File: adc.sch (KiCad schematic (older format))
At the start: 19 parts, among them J15 Conn_01x04_Male, U22 AD7960BCPZ-RL7, U23 OPA325

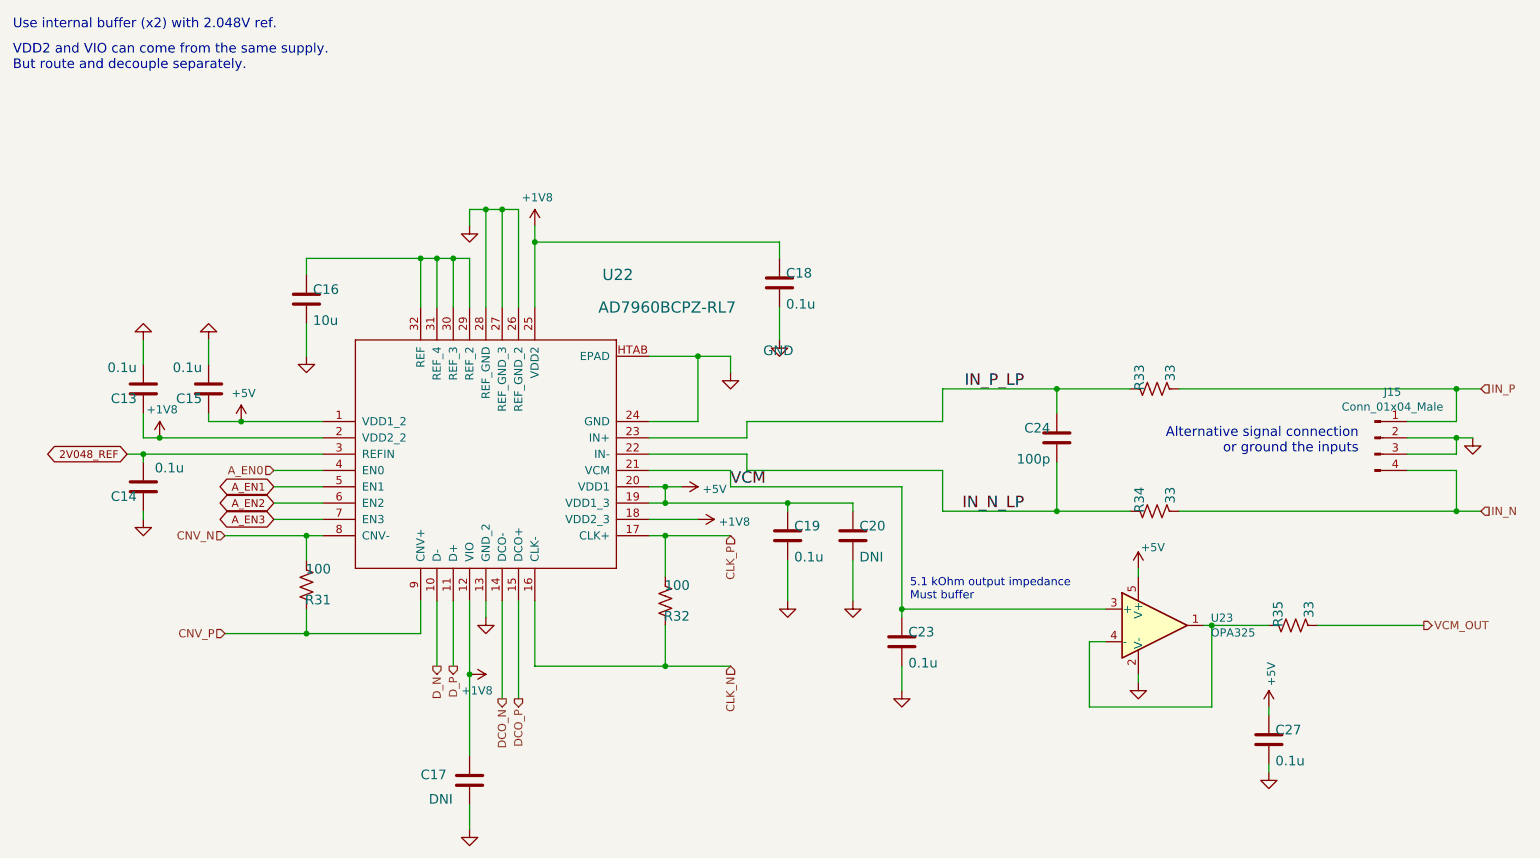
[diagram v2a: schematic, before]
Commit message: layout cleanup; removed custom footrpints
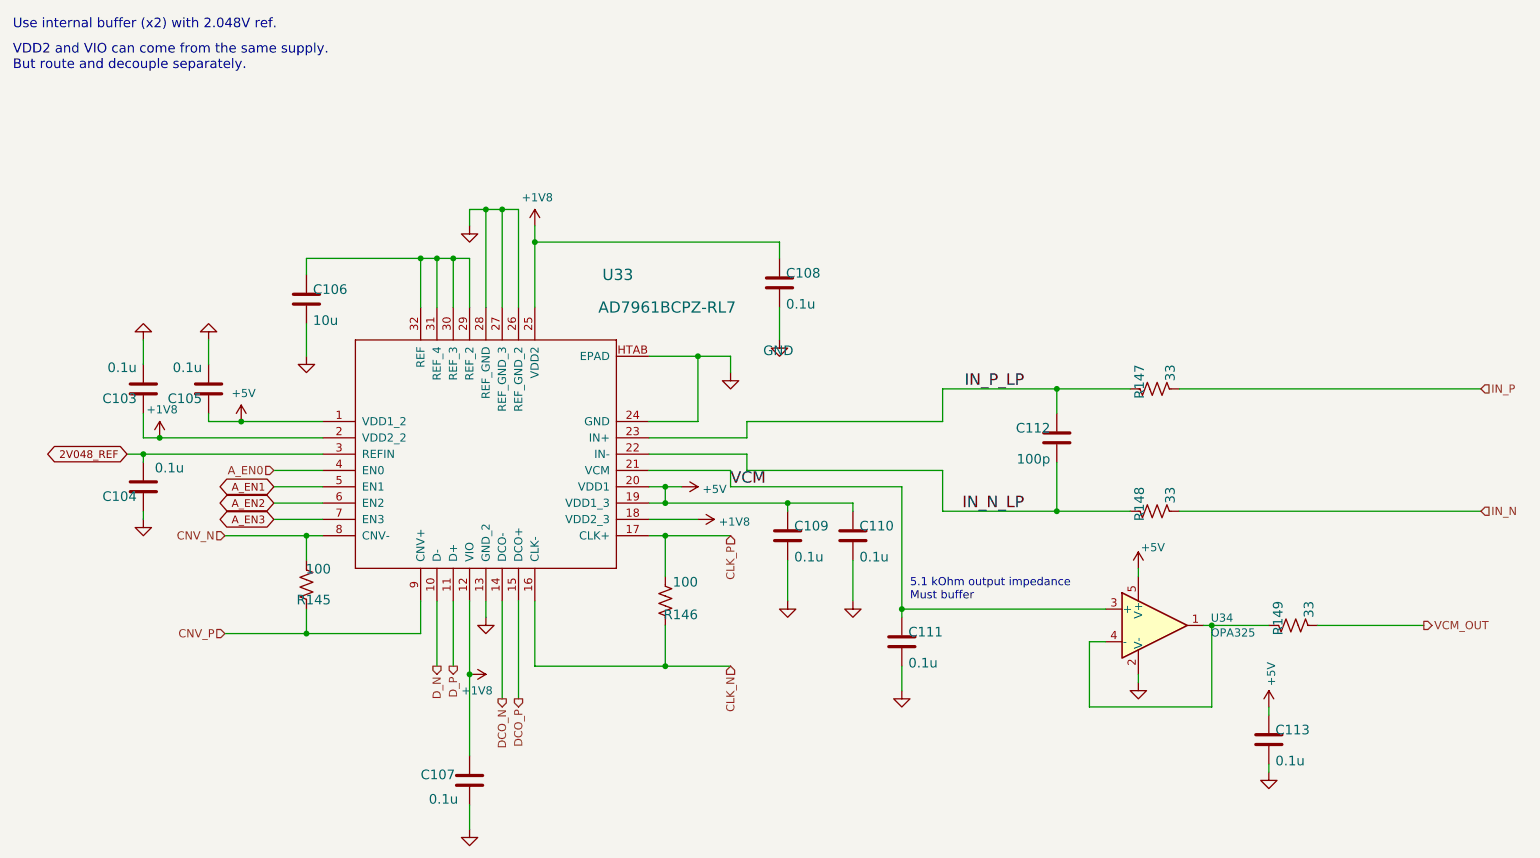
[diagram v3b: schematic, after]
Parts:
- removed J15: Conn_01x04_Male, Connector_PinHeader_2.54mm:PinHeader_1x04_P2.54mm_Vertical_SMD_Pin1Left, symbol Connector:Conn_01x04_Male
- C17, C20: value DNI -> 0.1u; Manf# (none) -> CL10B104KA8NFNC
- U22: value AD7960BCPZ-RL7 -> AD7961BCPZ-RL7; footprint adc_dac_v1:CP_32_7 -> Package_DFN_QFN:QFN-32-1EP_5x5mm_P0.5mm_EP3.1x3.1mm
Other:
- note removed: "Alternative signal connection\nor ground the inputs"
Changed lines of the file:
@@
 $Descr A 11000 8500
 encoding utf-8
-Sheet 6 18
+Sheet 8 18
 Title ""
 Date ""
@@
 AR Path="/60BF7757/B0DC2316" Ref="C69"  Part="1"
 AR Path="/60C1F416/B0DC2316" Ref="C112"  Part="1"
-F 0 "C24" H 7090 3725 59  0000 L BNN
+F 0 "C112" H 7090 3725 59  0000 L BNN
 F 1 "100p" H 7090 3535 59  0000 L BNN
 F 2 "Capacitor_SMD:C_0603_1608Metric" H 7050 3700 50  0001 C CNN
@@
 AR Path="/60BF7757/B996151F" Ref="R140"  Part="1"
 AR Path="/60C1F416/B996151F" Ref="R145"  Part="1"
-F 0 "R31" H 2300 4659 59  0000 L BNN
+F 0 "R145" H 2300 4659 59  0000 L BNN
 F 1 "100" H 2300 4470 59  0000 L BNN
 F 2 "Resistor_SMD:R_0603_1608Metric" H 2450 4600 50  0001 C CNN
@@
 AR Path="/60BF7757/56DFCCD0" Ref="C65"  Part="1"
 AR Path="/60C1F416/56DFCCD0" Ref="C108"  Part="1"
-F 0 "C18" H 5390 2775 59  0000 L BNN
+F 0 "C108" H 5390 2775 59  0000 L BNN
 F 1 "0.1u" H 5390 2585 59  0000 L BNN
 F 2 "Capacitor_SMD:C_0603_1608Metric" H 5350 2750 50  0001 C CNN
@@
 AR Path="/60BF7757/BF33D434" Ref="R141"  Part="1"
 AR Path="/60C1F416/BF33D434" Ref="R146"  Part="1"
-F 0 "R32" H 4500 4759 59  0000 L BNN
-F 1 "100" H 4500 4570 59  0000 L BNN
+F 0 "R146" H 4450 4750 59  0000 L BNN
+F 1 "100" H 4450 4550 59  0000 L BNN
 F 2 "Resistor_SMD:R_0603_1608Metric" H 4650 4700 50  0001 C CNN
 F 3 "" H 4650 4700 50  0001 C CNN
@@
 AR Path="/60BF7757/C9238E33" Ref="C66"  Part="1"
 AR Path="/60C1F416/C9238E33" Ref="C109"  Part="1"
-F 0 "C19" H 5440 4325 59  0000 L BNN
+F 0 "C109" H 5440 4325 59  0000 L BNN
 F 1 "0.1u" H 5440 4135 59  0000 L BNN
 F 2 "Capacitor_SMD:C_0603_1608Metric" H 5400 4300 50  0001 C CNN
@@
 AR Path="/60BF7757/E612D2BB" Ref="C67"  Part="1"
 AR Path="/60C1F416/E612D2BB" Ref="C110"  Part="1"
-F 0 "C20" H 5840 4325 59  0000 L BNN
-F 1 "DNI" H 5840 4135 59  0000 L BNN
+F 0 "C110" H 5840 4325 59  0000 L BNN
+F 1 "0.1u" H 5840 4135 59  0000 L BNN
 F 2 "Capacitor_SMD:C_0603_1608Metric" H 5800 4300 50  0001 C CNN
 F 3 "" H 5800 4300 50  0001 C CNN
+F 4 "CL10B104KA8NFNC" H 5800 4300 50  0001 C CNN "Manf#"
 	1    5800 4300
 	1    0    0    -1
@@
 AR Path="/60BF7757/1FADEAAB" Ref="C60"  Part="1"
 AR Path="/60C1F416/1FADEAAB" Ref="C103"  Part="1"
-F 0 "C13" H 1490 3425 59  0000 L BNN
+F 0 "C103" H 1490 3425 59  0000 L BNN
 F 1 "0.1u" H 1490 3235 59  0000 L BNN
 F 2 "Capacitor_SMD:C_0603_1608Metric" H 1450 3400 50  0001 C CNN
@@
 AR Path="/60BF7757/9D5B9004" Ref="C62"  Part="1"
 AR Path="/60C1F416/9D5B9004" Ref="C105"  Part="1"
-F 0 "C15" H 1890 3425 59  0000 L BNN
+F 0 "C105" H 1890 3425 59  0000 L BNN
 F 1 "0.1u" H 1890 3235 59  0000 L BNN
 F 2 "Capacitor_SMD:C_0603_1608Metric" H 1850 3400 50  0001 C CNN
@@
 AR Path="/60BF7757/87DF8B8E" Ref="R142"  Part="1"
 AR Path="/60C1F416/87DF8B8E" Ref="R147"  Part="1"
-F 0 "R33" H 7500 3459 59  0000 L BNN
+F 0 "R147" H 7500 3459 59  0000 L BNN
 F 1 "33" H 7500 3270 59  0000 L BNN
 F 2 "Resistor_SMD:R_0603_1608Metric" H 7650 3400 50  0001 C CNN
@@
 AR Path="/60BF7757/BFC3FA38" Ref="R143"  Part="1"
 AR Path="/60C1F416/BFC3FA38" Ref="R148"  Part="1"
-F 0 "R34" H 7500 4209 59  0000 L BNN
+F 0 "R148" H 7500 4209 59  0000 L BNN
 F 1 "33" H 7500 4020 59  0000 L BNN
 F 2 "Resistor_SMD:R_0603_1608Metric" H 7650 4150 50  0001 C CNN
@@
 $EndComp
 $Comp
-L power:GND #GND0124
-U 1 1 5F8B303C
-P 9600 3700
-AR Path="/6095A697/5F8B303C" Ref="#GND0124"  Part="1"
-AR Path="/60BE6CE5/5F8B303C" Ref="#GND0217"  Part="1"
-AR Path="/60BF7757/5F8B303C" Ref="#GND0232"  Part="1"
-AR Path="/60C1F416/5F8B303C" Ref="#GND0247"  Part="1"
-F 0 "#GND0247" H 9600 3700 50  0001 C CNN
-F 1 "GND" H 9500 3600 59  0001 L BNN
-F 2 "" H 9600 3700 50  0001 C CNN
-F 3 "" H 9600 3700 50  0001 C CNN
-	1    9600 3700
-	-1   0    0    -1
-$EndComp
-$Comp
 L Device:C C17
 U 1 1 E8572435
@@
 AR Path="/60BF7757/E8572435" Ref="C64"  Part="1"
 AR Path="/60C1F416/E8572435" Ref="C107"  Part="1"
-F 0 "C17" H 3150 5800 59  0000 L BNN
-F 1 "DNI" H 3200 5650 59  0000 L BNN
+F 0 "C107" H 3150 5800 59  0000 L BNN
+F 1 "0.1u" H 3200 5650 59  0000 L BNN
 F 2 "Capacitor_SMD:C_0603_1608Metric" H 3450 5800 50  0001 C CNN
 F 3 "" H 3450 5800 50  0001 C CNN
+F 4 "CL10B104KA8NFNC" H 3450 5800 50  0001 C CNN "Manf#"
 	1    3450 5800
 	1    0    0    -1
@@
 AR Path="/60BF7757/70C280EF" Ref="U31"  Part="1"
 AR Path="/60C1F416/70C280EF" Ref="U33"  Part="1"
-F 0 "U22" H 4264 4859 69  0000 L BNN
-F 1 "AD7960BCPZ-RL7" H 4239 4659 69  0000 L BNN
-F 2 "adc_dac_v1:CP_32_7" H 3550 3800 50  0001 C CNN
+F 0 "U33" H 4264 4859 69  0000 L BNN
+F 1 "AD7961BCPZ-RL7" H 4239 4659 69  0000 L BNN
+F 2 "Package_DFN_QFN:QFN-32-1EP_5x5mm_P0.5mm_EP3.1x3.1mm" H 3550 3800 50  0001 C CNN
 F 3 "" H 3550 3800 50  0001 C CNN
 F 4 "AD7961BCPZ-RL7" H 4264 4959 50  0001 C CNN "Manf#"
@@
 AR Path="/60BF7757/32508C8E" Ref="C63"  Part="1"
 AR Path="/60C1F416/32508C8E" Ref="C106"  Part="1"
-F 0 "C16" H 2490 2875 59  0000 L BNN
+F 0 "C106" H 2490 2875 59  0000 L BNN
 F 1 "10u" H 2490 2685 59  0000 L BNN
 F 2 "Capacitor_SMD:C_0603_1608Metric" H 2450 2850 50  0001 C CNN
@@
 AR Path="/60BF7757/60CEDBBA" Ref="U32"  Part="1"
 AR Path="/60C1F416/60CEDBBA" Ref="U34"  Part="1"
-F 0 "U23" H 7994 4896 50  0000 L CNN
+F 0 "U34" H 7994 4896 50  0000 L CNN
 F 1 "OPA325" H 7994 4805 50  0000 L CNN
 F 2 "Package_TO_SOT_SMD:SOT-23-5" H 7550 4650 50  0001 L CNN
@@
 AR Path="/60BF7757/60D076A5" Ref="R144"  Part="1"
 AR Path="/60C1F416/60D076A5" Ref="R149"  Part="1"
-F 0 "R35" H 8350 4909 59  0000 L BNN
+F 0 "R149" H 8350 4909 59  0000 L BNN
 F 1 "33" H 8350 4720 59  0000 L BNN
 F 2 "Resistor_SMD:R_0603_1608Metric" H 8500 4850 50  0001 C CNN
@@
 AR Path="/60BF7757/60D0F62A" Ref="C102"  Part="1"
 AR Path="/60C1F416/60D0F62A" Ref="C113"  Part="1"
-F 0 "C27" H 8390 5575 59  0000 L BNN
+F 0 "C113" H 8390 5575 59  0000 L BNN
 F 1 "0.1u" H 8390 5385 59  0000 L BNN
 F 2 "Capacitor_SMD:C_0603_1608Metric" H 8350 5550 50  0001 C CNN
@@
 AR Path="/60BF7757/60D49EBB" Ref="C61"  Part="1"
 AR Path="/60C1F416/60D49EBB" Ref="C104"  Part="1"
-F 0 "C14" H 1490 4025 59  0000 L BNN
+F 0 "C104" H 1490 4025 59  0000 L BNN
 F 1 "0.1u" H 1200 3850 59  0000 L BNN
 F 2 "Capacitor_SMD:C_0603_1608Metric" H 1450 4000 50  0001 C CNN
@@
 AR Path="/60BF7757/60D51F18" Ref="C68"  Part="1"
 AR Path="/60C1F416/60D51F18" Ref="C111"  Part="1"
-F 0 "C23" H 6140 4975 59  0000 L BNN
+F 0 "C111" H 6140 4975 59  0000 L BNN
 F 1 "0.1u" H 6140 4785 59  0000 L BNN
 F 2 "Capacitor_SMD:C_0603_1608Metric" H 6100 4950 50  0001 C CNN
@@
 F 3 "" H 6100 5250 50  0001 C CNN
 	1    6100 5250
-	1    0    0    -1
-$EndComp
-$Comp
-L Connector:Conn_01x04_Male J15
-U 1 1 628E78F9
-P 9000 3700
-AR Path="/6095A697/628E78F9" Ref="J15"  Part="1"
-AR Path="/60BE6CE5/628E78F9" Ref="J17"  Part="1"
-AR Path="/60BF7757/628E78F9" Ref="J18"  Part="1"
-AR Path="/60C1F416/628E78F9" Ref="J19"  Part="1"
-F 0 "J15" H 9108 3981 50  0000 C CNN
-F 1 "Conn_01x04_Male" H 9108 3890 50  0000 C CNN
-F 2 "Connector_PinHeader_2.54mm:PinHeader_1x04_P2.54mm_Vertical_SMD_Pin1Left" H 9000 3700 50  0001 C CNN
-F 3 "~" H 9000 3700 50  0001 C CNN
-F 4 "54201-G0804LF" H 9000 3700 50  0001 C CNN "Manf#"
-	1    9000 3700
 	1    0    0    -1
 $EndComp
@@
 Text Notes 650  1450 0    59   ~ 0
 VDD2 and VIO can come from the same supply. \nBut route and decouple separately.
-Text Notes 8900 3800 2    59   ~ 0
-Alternative signal connection\nor ground the inputs
 Text Label 6850 4150 2    70   ~ 0
 IN_N_LP
@@
 	5050 3900 5050 4000
 Wire Wire Line
-	9500 3900 9200 3900
-Wire Wire Line
-	9500 3600 9200 3600
-Wire Wire Line
 	3450 2900 3450 2600
 Wire Wire Line
@@
 	2550 3800 1450 3800
 Wire Wire Line
-	9200 3700 9500 3700
-Wire Wire Line
-	9500 3700 9600 3700
-Wire Wire Line
-	9500 3800 9500 3700
-Wire Wire Line
-	9500 3800 9200 3800
-Wire Wire Line
 	3850 2900 3850 2500
 Wire Wire Line
@@
 	4750 4000 4650 4000
 Wire Wire Line
-	9500 3900 9500 4150
-Wire Wire Line
-	9500 3400 9500 3600
-Wire Wire Line
-	9500 3400 7800 3400
-Wire Wire Line
 	7050 3850 7050 4150
 Wire Wire Line
-	9500 4150 7800 4150
-Wire Wire Line
 	6350 3900 6350 4150
 Wire Wire Line
@@
 Wire Wire Line
 	6350 3400 7050 3400
-Wire Wire Line
-	9500 4150 9650 4150
-Wire Wire Line
-	9500 3400 9650 3400
 Wire Wire Line
 	6100 4000 6100 4750
@@
 Connection ~ 3650 2300
 Connection ~ 4850 3200
-Connection ~ 9500 3700
 Connection ~ 4650 5100
 Connection ~ 4650 4300
@@
 Connection ~ 2050 3600
 Connection ~ 4650 4000
-Connection ~ 9500 4150
-Connection ~ 9500 3400
 Connection ~ 8000 4850
 Connection ~ 1450 3800
 Connection ~ 6100 4750
 Connection ~ 3850 2500
+Wire Wire Line
+	7800 4150 9650 4150
+Wire Wire Line
+	7800 3400 9650 3400
 $EndSCHEMATC

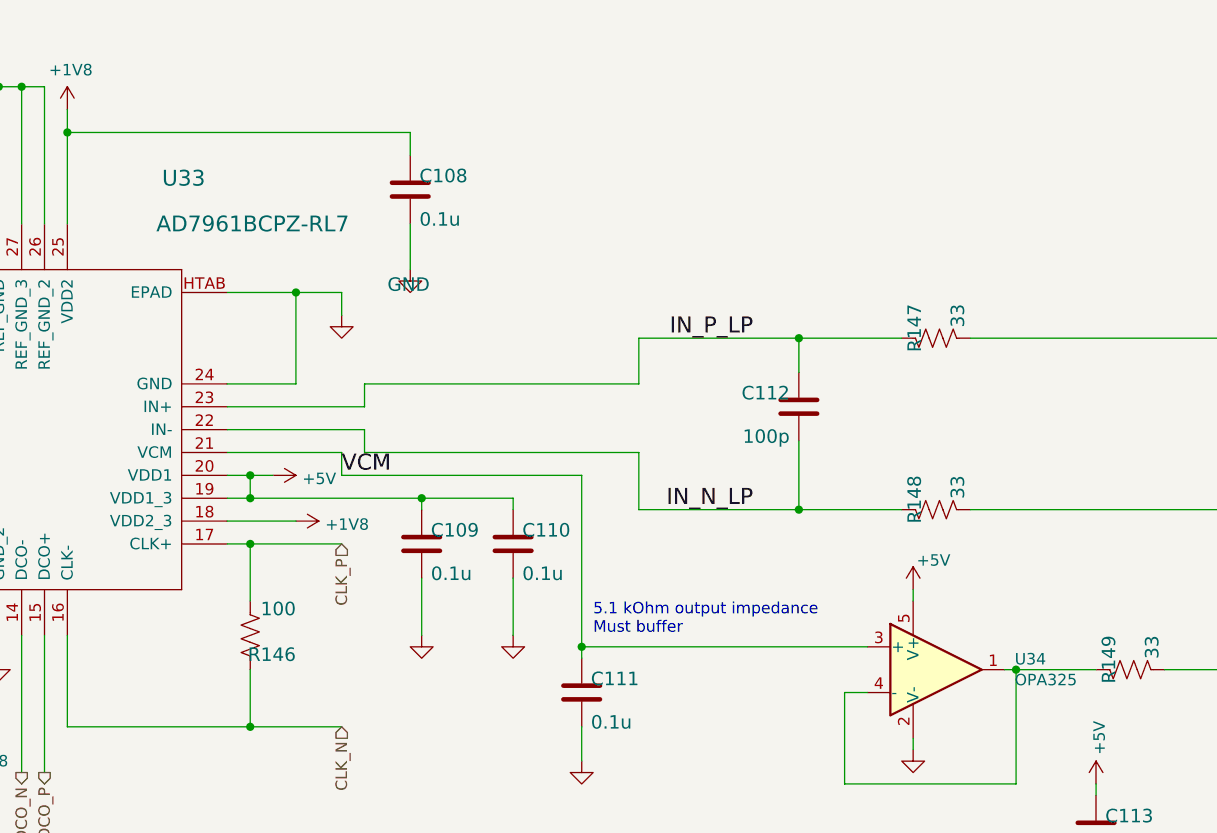
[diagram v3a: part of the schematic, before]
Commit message: updates of DAC part placement
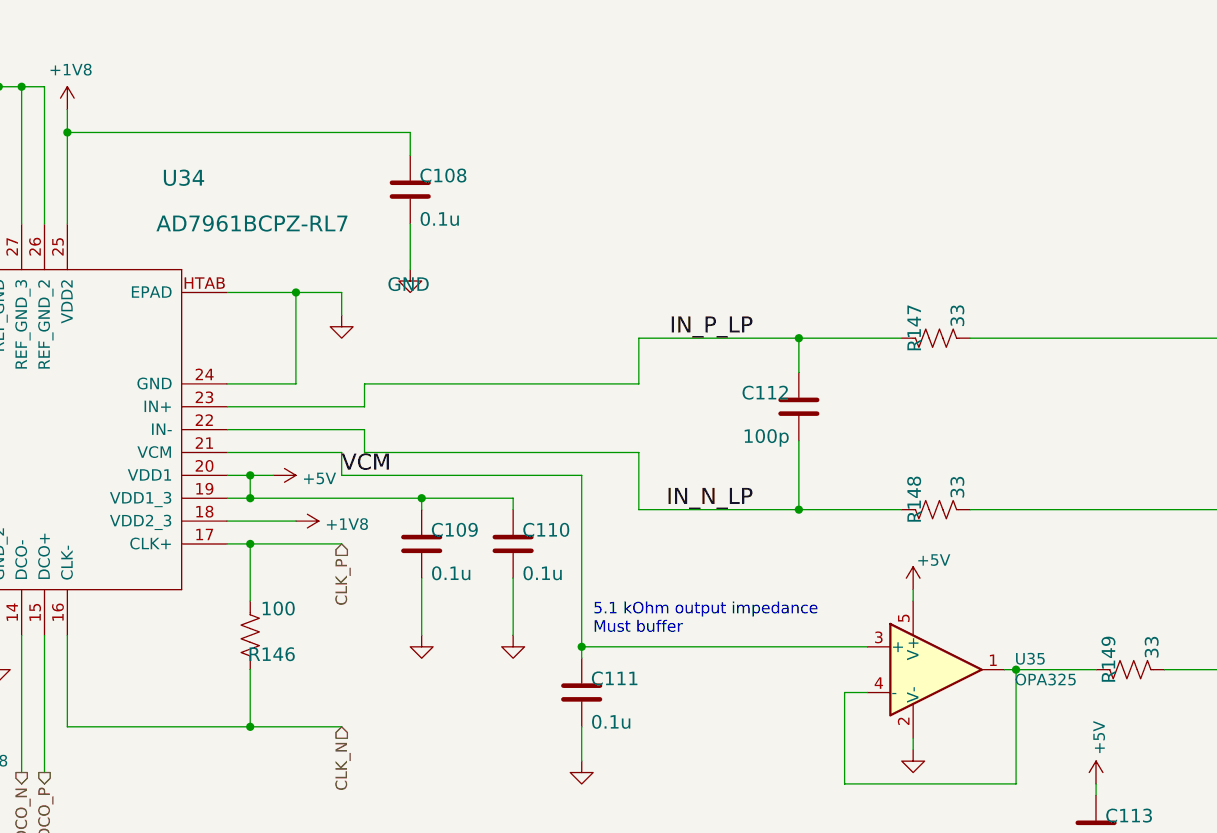
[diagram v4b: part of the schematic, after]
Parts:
- renumbered C13 to C38, C14 to C39, C15 to C40, C16 to C41, C17 to C42, C18 to C43, C19 to C44, C20 to C45, C23 to C46, C24 to C47, C27 to C48, R31 to R79, R32 to R80, R33 to R81, R34 to R82, R35 to R83, U22 to U28, U23 to U29

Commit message: updated component placement
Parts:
- U28: symbol adc_dac_v1-eagle-import:AD7960BCPZ-RL7 -> covg-kicad:AD7960BCPZ-RL7
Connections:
- net GND: now also U28.33 (EPAD); no longer U28.HTAB (EPAD)
